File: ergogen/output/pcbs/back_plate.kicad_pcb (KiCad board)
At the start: 2 copper layers, 144.2 x 91.9 mm, 6 parts

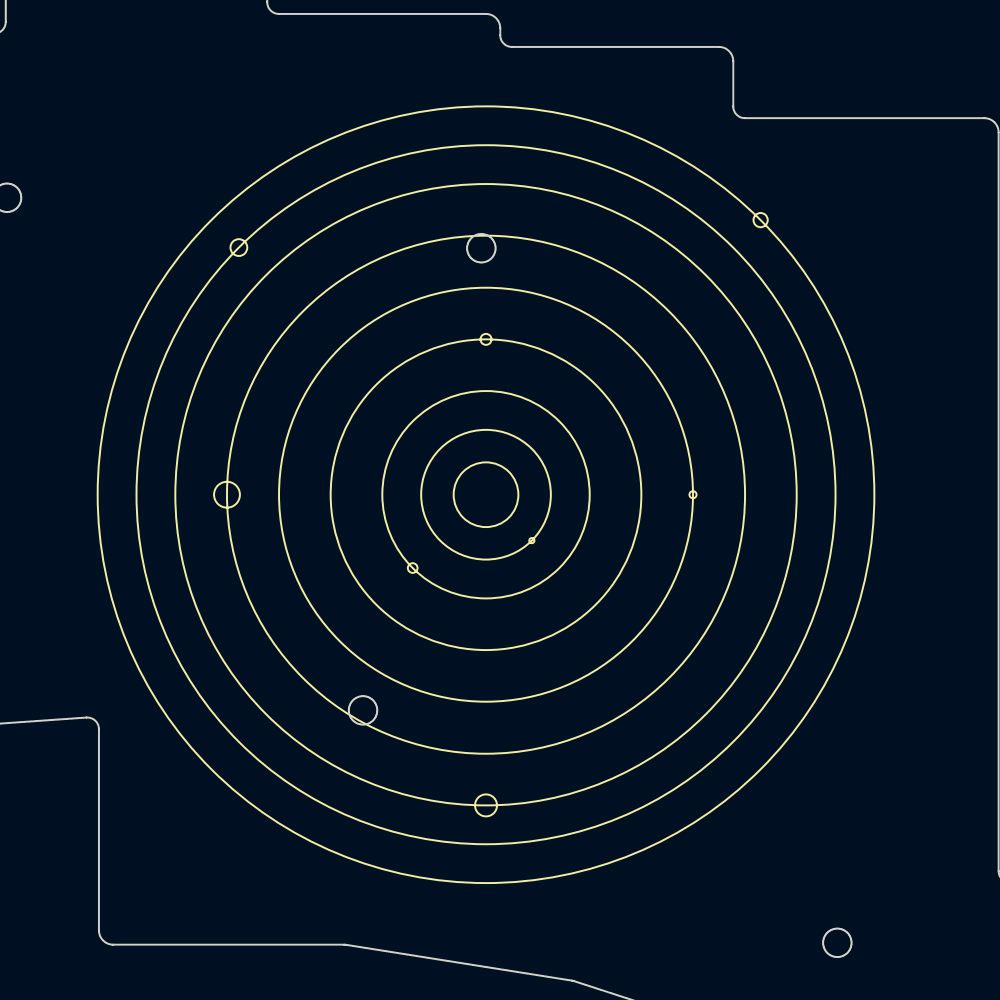
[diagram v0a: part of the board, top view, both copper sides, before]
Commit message: case and backplate updates
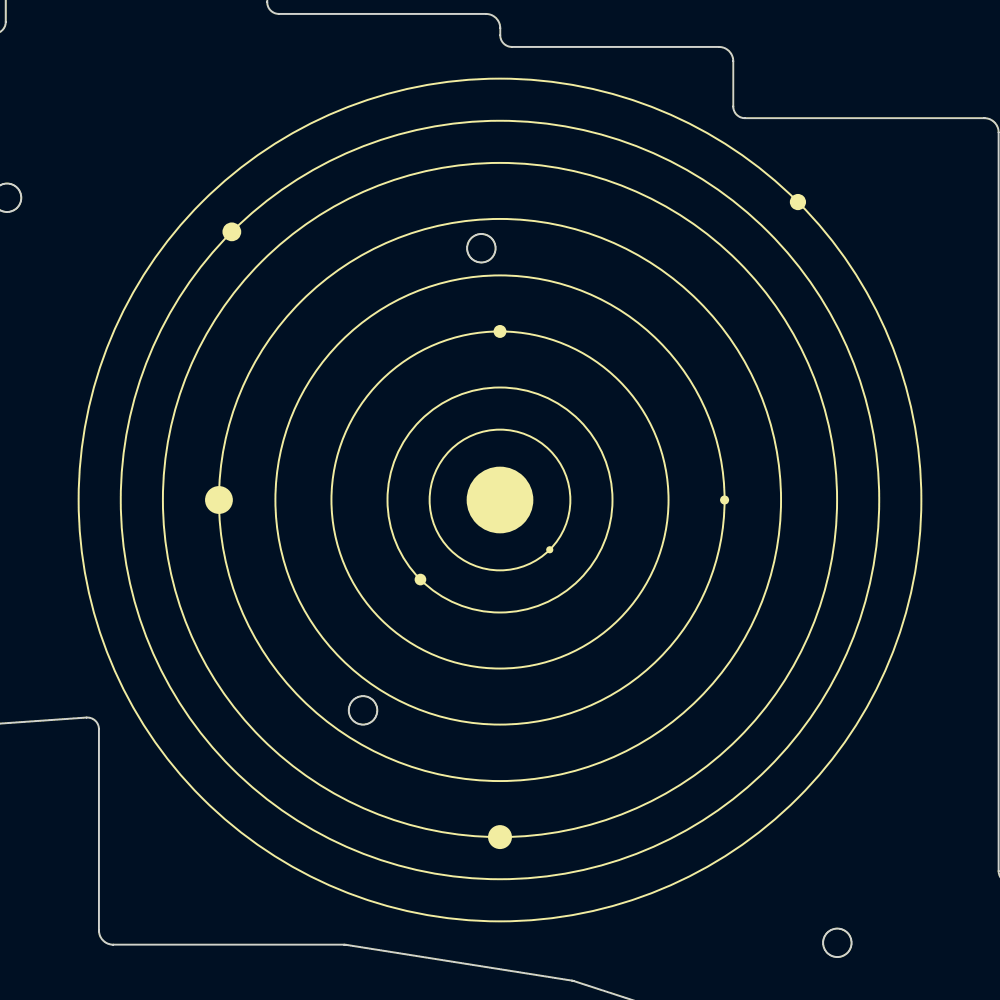
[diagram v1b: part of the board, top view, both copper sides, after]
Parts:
- moved ? 1.15 mm to (130.4, 72.4)
